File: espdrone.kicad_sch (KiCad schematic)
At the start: 56 parts, among them U2 USBLC6-2P6, U3 W25Q128JVP, Y1 Crystal_GND24

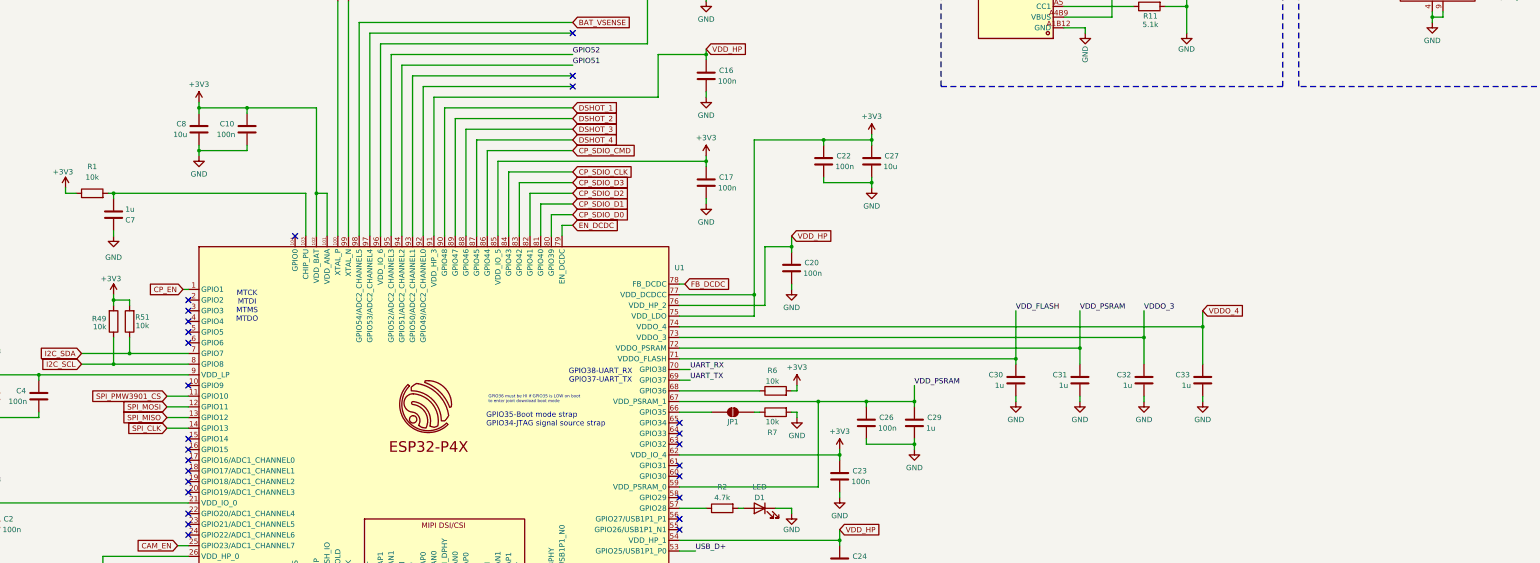
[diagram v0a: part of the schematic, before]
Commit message: Lots of FC routing
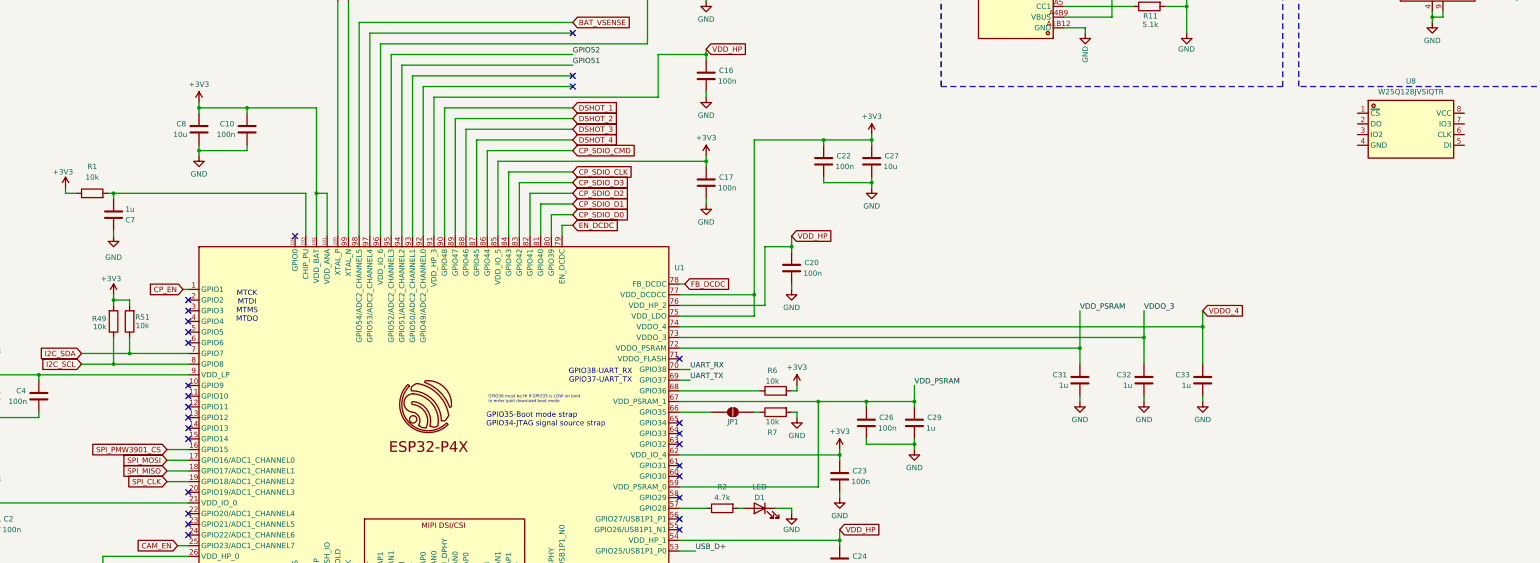
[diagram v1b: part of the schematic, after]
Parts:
- removed C30: 1u, Capacitor_SMD:C_0402_1005Metric, symbol Device:C
- added U8: W25Q128JVSIQTR, easyeda2kicad:SOIC-8_L5.3-W5.3-P1.27-LS8.0-BL, symbol easyeda2kicad:W25Q128JVSIQTR
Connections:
- net SPI_CLK: now also U1.19 (GPIO18/ADC1_CHANNEL2); no longer U1.14 (GPIO13)
- net SPI_MISO: now also U1.18 (GPIO17/ADC1_CHANNEL1); no longer U1.13 (GPIO12)
- net SPI_MOSI: now also U1.17 (GPIO16/ADC1_CHANNEL0); no longer U1.12 (GPIO11)
- net SPI_PMW3901_CS: now also U1.16 (GPIO15); no longer U1.11 (GPIO10)
- net VDD_FLASH: no longer U1.71 (VDDO_FLASH)
- no-connect marks 42 -> 43

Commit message: Duplicate ESC layout
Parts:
- D1: footprint LED_SMD:LED_0402_1005Metric -> LED_SMD:LED_0201_0603Metric
- R2: footprint Resistor_SMD:R_0402_1005Metric -> Resistor_SMD:R_0201_0603Metric
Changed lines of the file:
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@@
 			)
 		)
-		(property "Footprint" "LED_SMD:LED_0402_1005Metric"
+		(property "Footprint" "LED_SMD:LED_0201_0603Metric"
 			(at 209.55 189.23 0)
 			(hide yes)
@@
 			)
 		)
-		(property "Footprint" "Resistor_SMD:R_0402_1005Metric"
+		(property "Footprint" "Resistor_SMD:R_0201_0603Metric"
 			(at 200.66 187.452 90)
 			(hide yes)

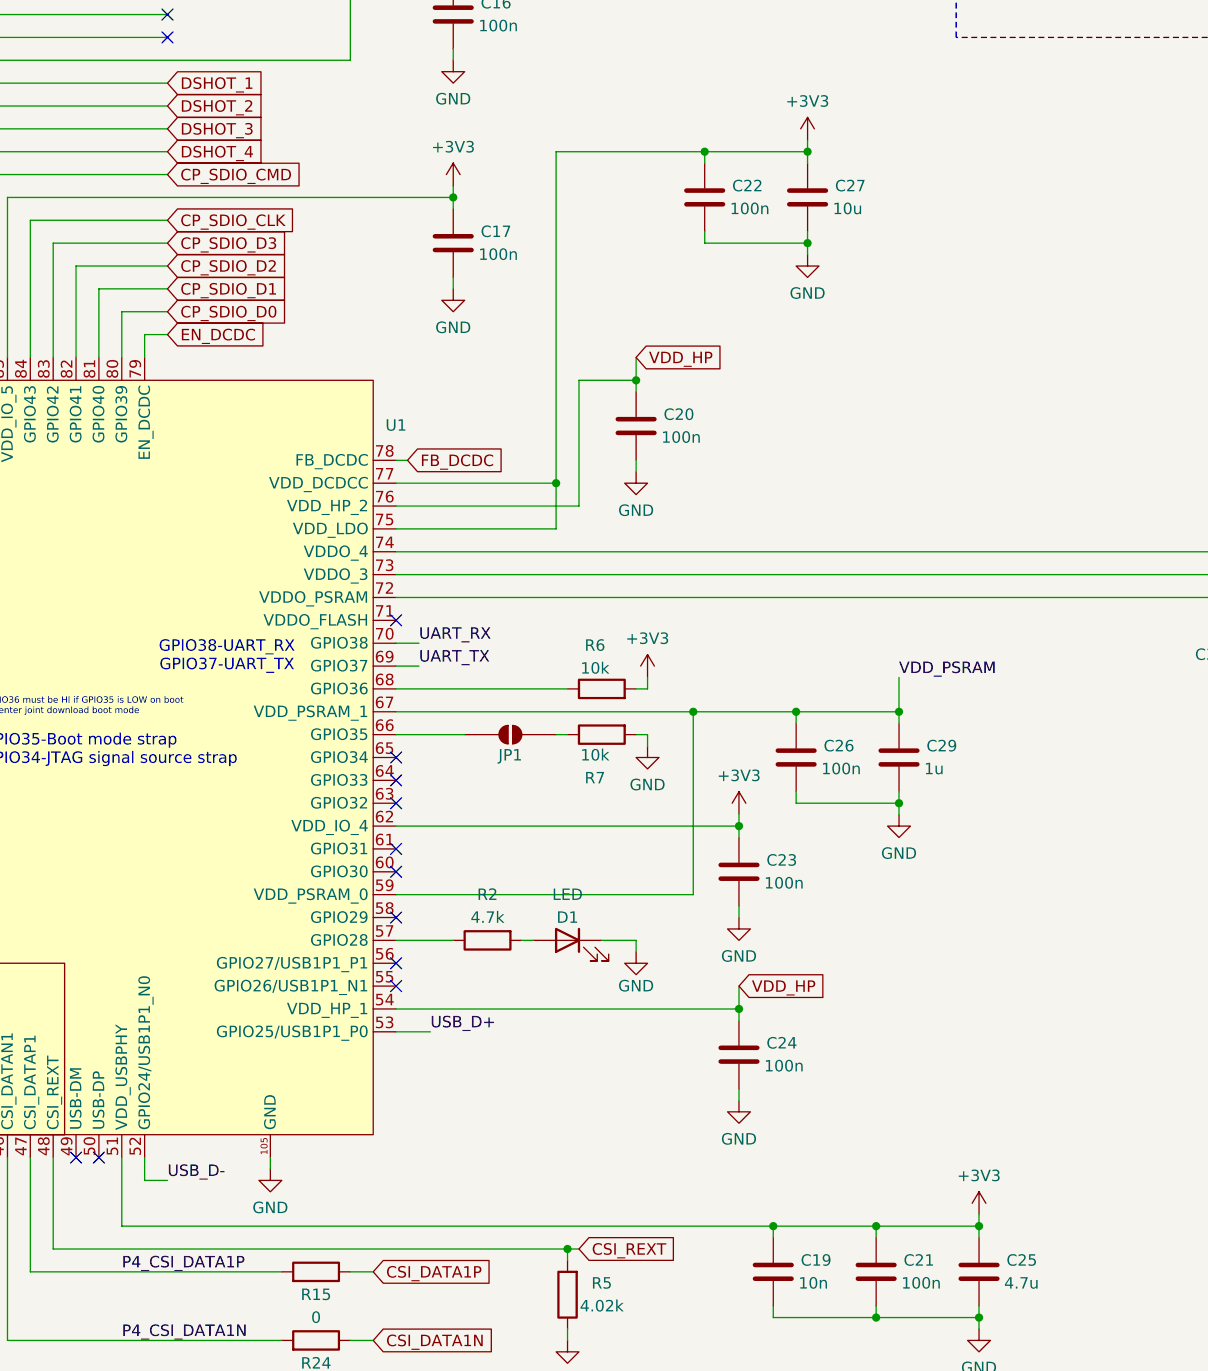
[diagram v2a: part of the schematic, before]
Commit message: Move P4 SDIO pins
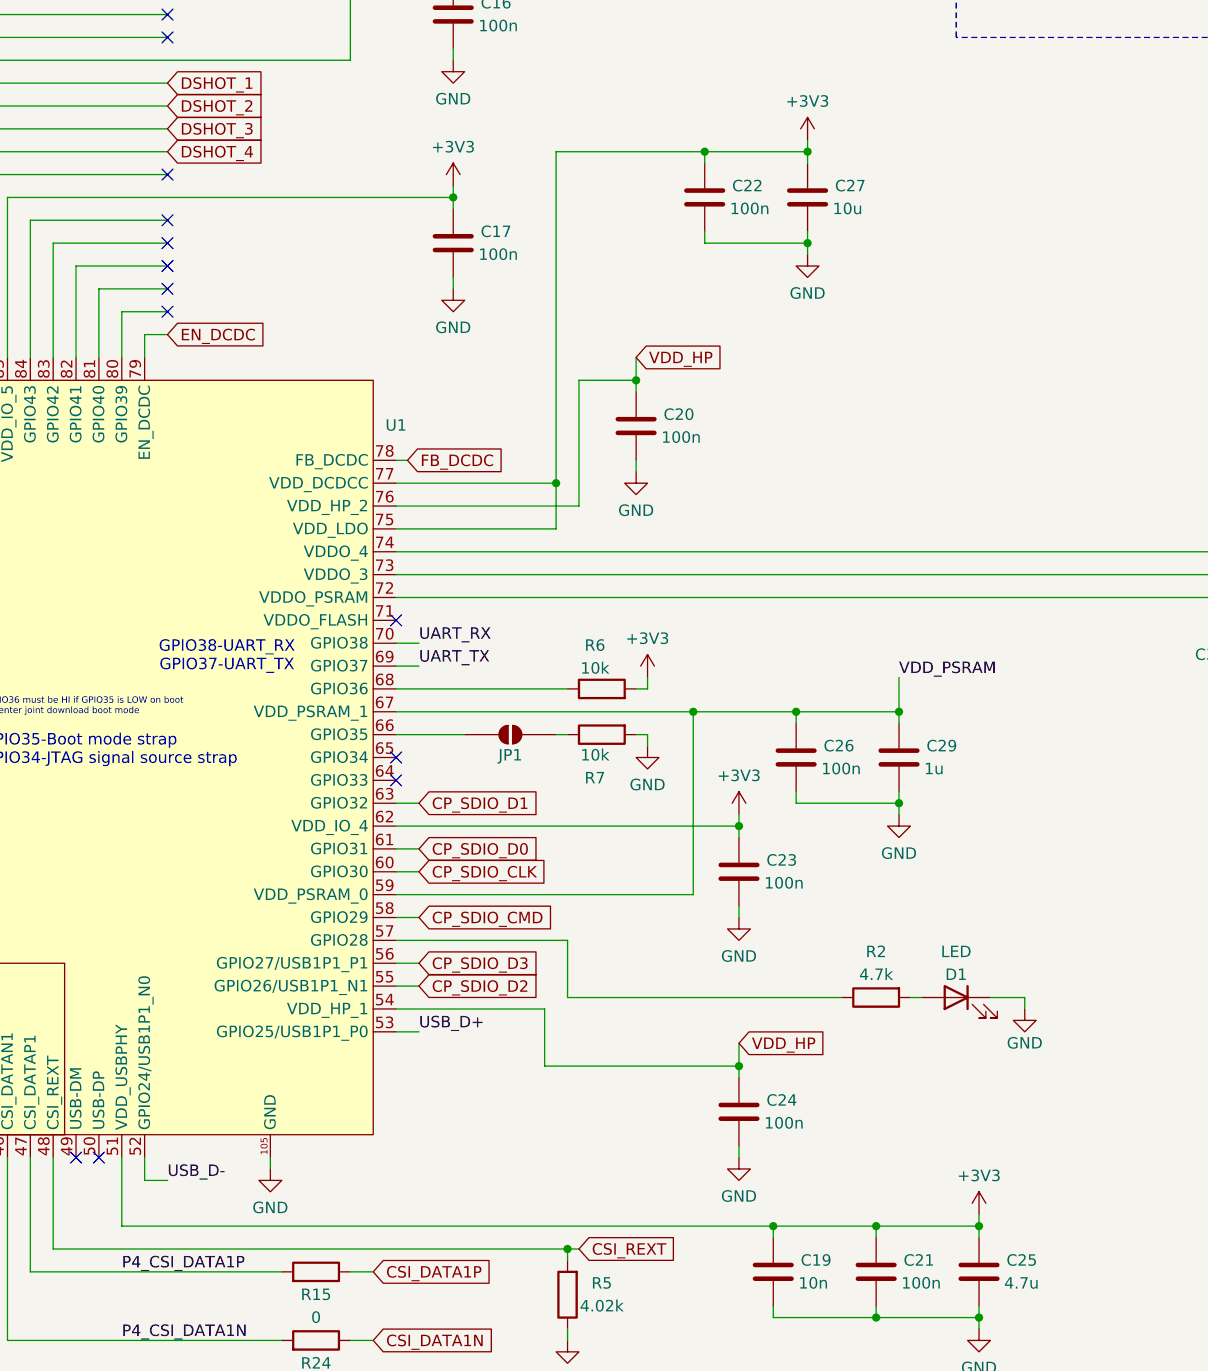
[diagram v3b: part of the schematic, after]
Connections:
- net CP_SDIO_CLK: now also U1.60 (GPIO30); no longer U1.84 (GPIO43)
- net CP_SDIO_CMD: now also U1.58 (GPIO29); no longer U1.86 (GPIO44)
- net CP_SDIO_D0: now also U1.61 (GPIO31); no longer U1.80 (GPIO39)
- net CP_SDIO_D1: now also U1.63 (GPIO32); no longer U1.81 (GPIO40)
- net CP_SDIO_D2: now also U1.55 (GPIO26/USB1P1_N1); no longer U1.82 (GPIO41)
- net CP_SDIO_D3: now also U1.56 (GPIO27/USB1P1_P1); no longer U1.83 (GPIO42)
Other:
- moved on the sheet: C24, D1, R2

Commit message: Group FC stuff
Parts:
- removed U8: W25Q128JVSIQTR, easyeda2kicad:SOIC-8_L5.3-W5.3-P1.27-LS8.0-BL, symbol easyeda2kicad:W25Q128JVSIQTR
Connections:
- net +3V3: now also C5.1, U1.30 (VDD_FLASH_IO)
- net VDD_FLASH: no longer C5.1, U1.30 (VDD_FLASH_IO)
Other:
- moved on the sheet: C31, C32, C33

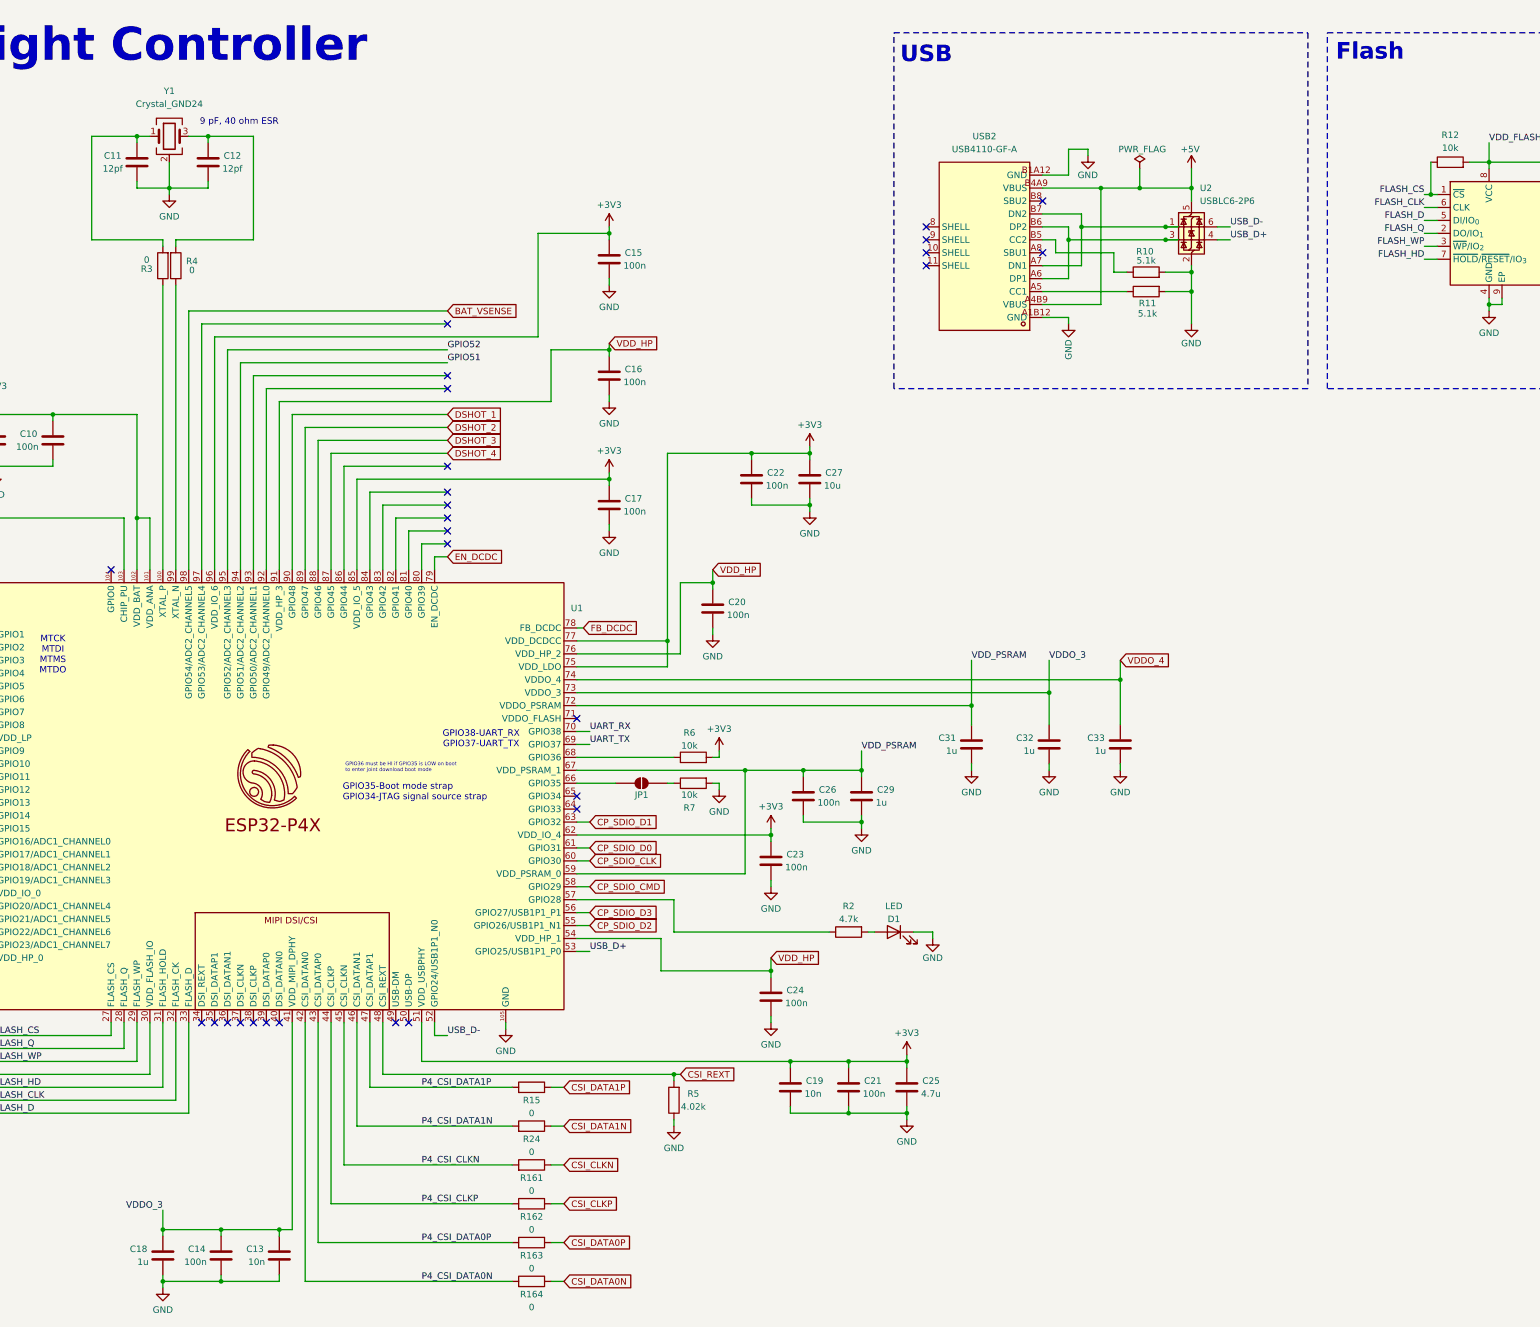
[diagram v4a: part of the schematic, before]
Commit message: Split FC stuff into subgroups
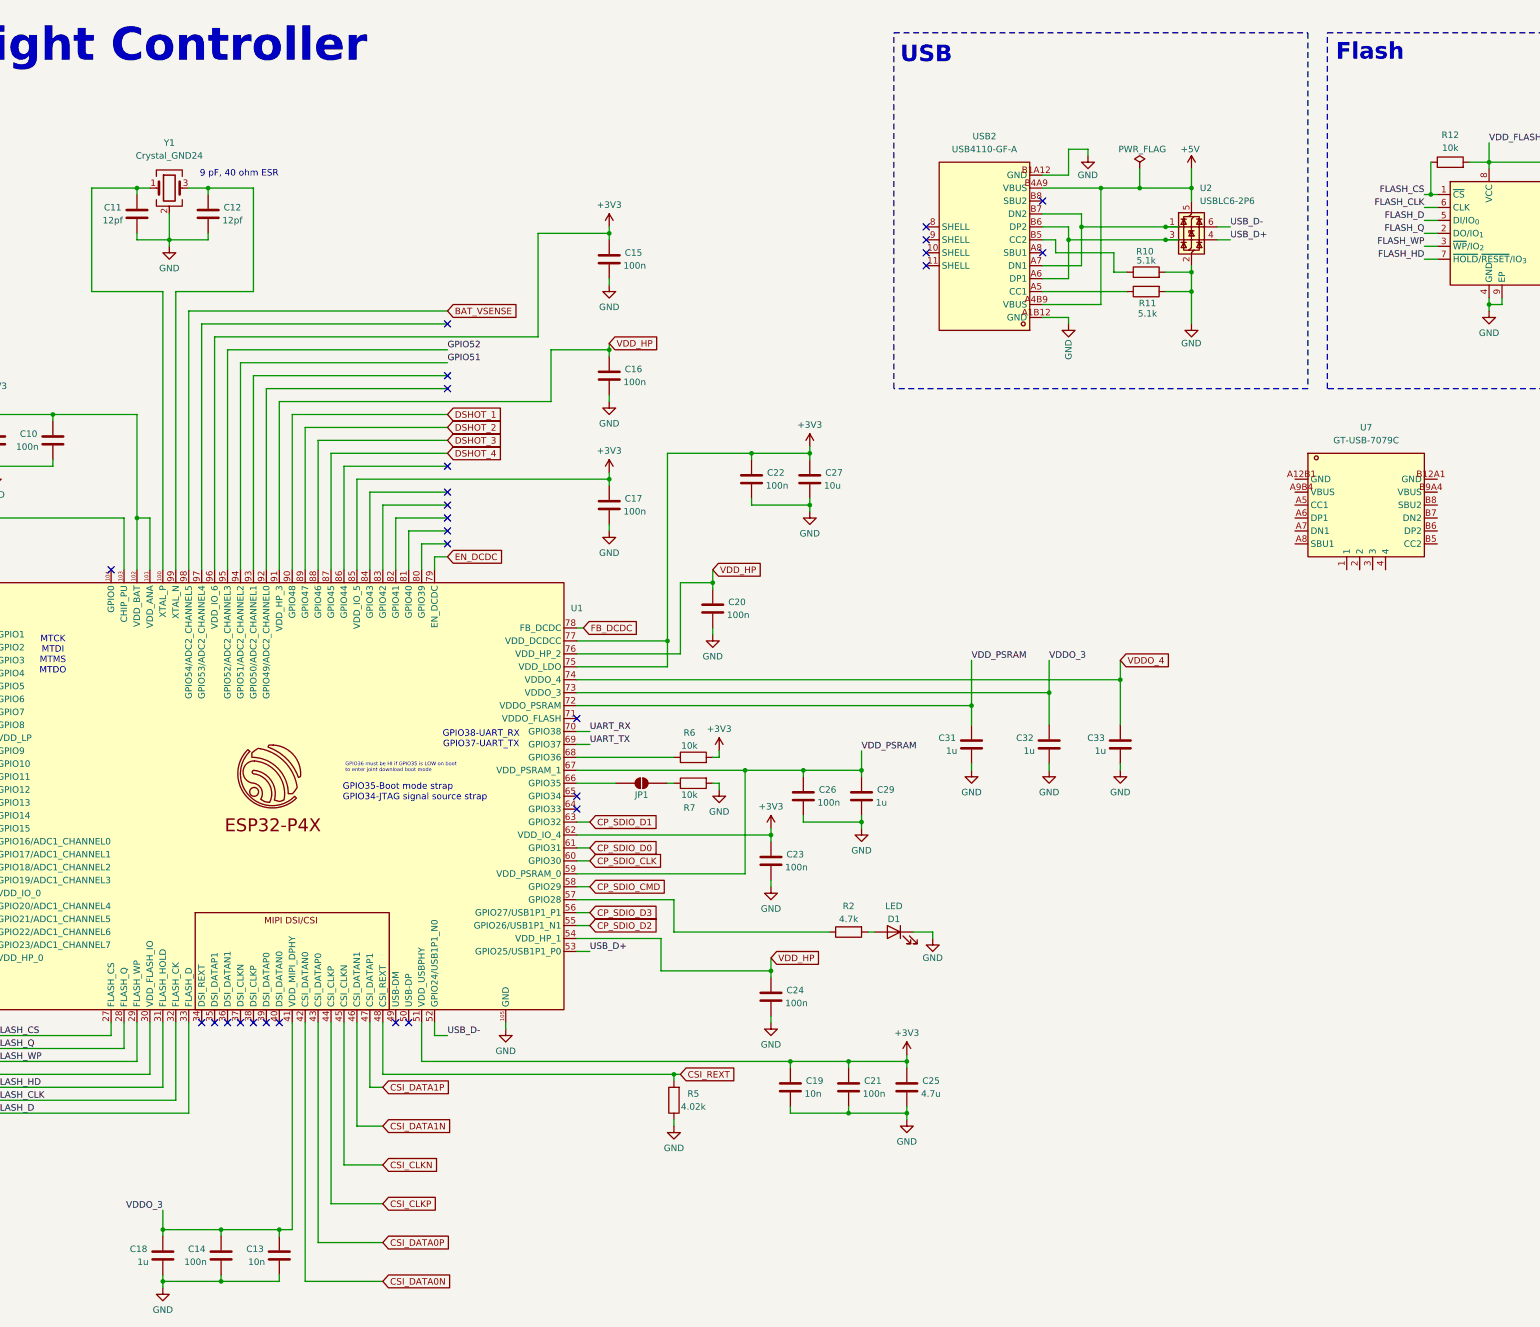
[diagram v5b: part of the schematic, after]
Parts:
- removed R15, R161, R162, R163, R164, R24: 0, Resistor_SMD:R_0201_0603Metric, symbol Device:R
- removed R3, R4: 0, Resistor_SMD:R_0402_1005Metric, symbol Device:R
- added U7: GT-USB-7079C, easyeda2kicad:TYPE-C-SMD_GT-USB-7079C, symbol easyeda2kicad:GT-USB-7079C
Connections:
- net P4_CSI_CLKN is gone; now on net CSI_CLKN: U1.45 (CSI_CLKN)
- net P4_CSI_CLKP is gone; now on net CSI_CLKP: U1.44 (CSI_CLKP)
- net P4_CSI_DATA0N is gone; now on net CSI_DATA0N: U1.42 (CSI_DATAN0)
- net P4_CSI_DATA0P is gone; now on net CSI_DATA0P: U1.43 (CSI_DATAP0)
- net P4_CSI_DATA1N is gone; now on net CSI_DATA1N: U1.46 (CSI_DATAN1)
- net P4_CSI_DATA1P is gone; now on net CSI_DATA1P: U1.47 (CSI_DATAP1)
- net at C12.1, Y1.3: now also U1.99 (XTAL_N)
- net at C11.1, Y1.1: now also U1.100 (XTAL_P)
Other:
- moved on the sheet: C11, C12, Y1

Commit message: Make P4 and C5 more compact
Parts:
- removed C5: 1u, Capacitor_SMD:C_0402_1005Metric, symbol Device:C
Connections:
- net +3V3: no longer U1.30 (VDD_FLASH_IO)
- no-connect marks 43 -> 44

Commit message: Good placement of most FC components
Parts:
- removed U2: USBLC6-2P6, Package_TO_SOT_SMD:SOT-666, symbol Power_Protection:USBLC6-2P6
- removed USB2: USB4110-GF-A, easyeda2kicad:USB-C-SMD_TYPE-C-16P-USB4110-GF-A, symbol easyeda2kicad:USB4110-GF-A
- added U15: TPD2EUSB30A, Package_TO_SOT_SMD:Texas_DRT-3, symbol Power_Protection:TPD2EUSB30A
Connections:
- net +5V: now also U7.A9B4 (VBUS), U7.B9A4 (VBUS)
- net GND: now also U7.A12B1 (GND), U7.B12A1 (GND), U15.3 (GND)
- net USB_D+: now also U7.A6 (DP1), U7.B6 (DP2), U15.1 (D+)
- net USB_D-: now also U7.A7 (DN1), U7.B7 (DN2), U15.2 (D-)
- net at R10.1: now also U7.B5 (CC2)
- net at U7.A5 (CC1): now also R11.1
- no-connect marks 44 -> 40
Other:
- moved on the sheet: R10, R11
